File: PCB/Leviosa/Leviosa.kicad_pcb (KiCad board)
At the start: 2 copper layers, 80 x 80 mm, 50 parts, among them J3 Conn_01x03, Q3 TIP122, Q4 TIP122, U1 LM324, U2 ATtiny13A-P, U3 TPS1H200AQDGNRQ1, U5 L7805, U6 SS495A

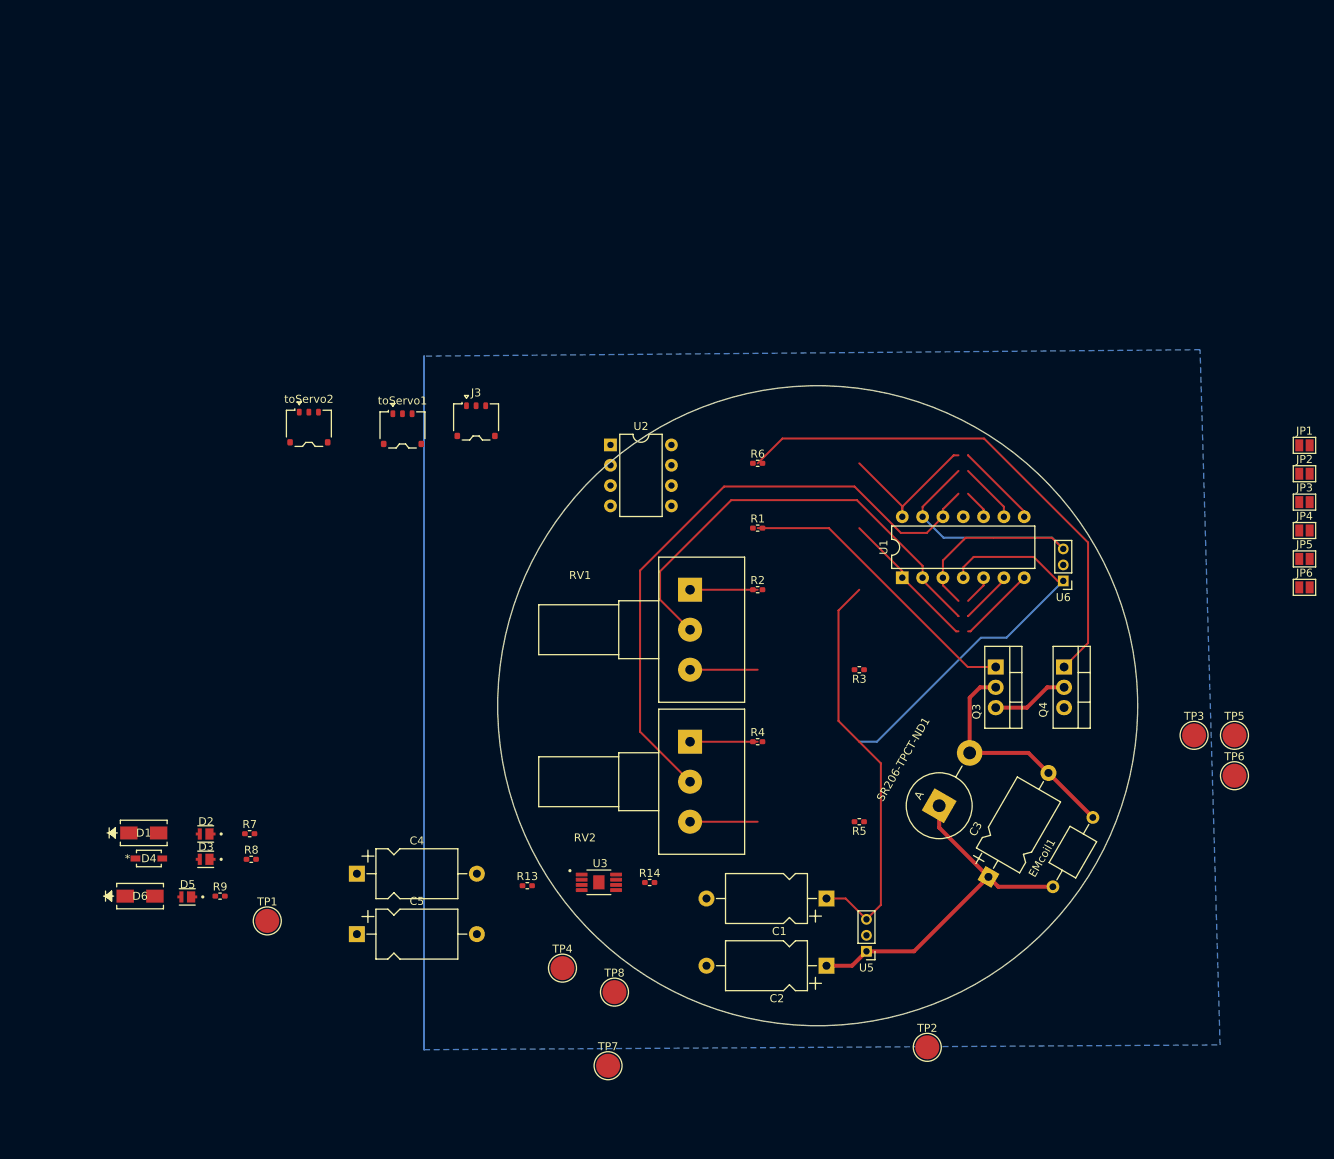
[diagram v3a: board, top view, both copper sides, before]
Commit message: update diode footprint
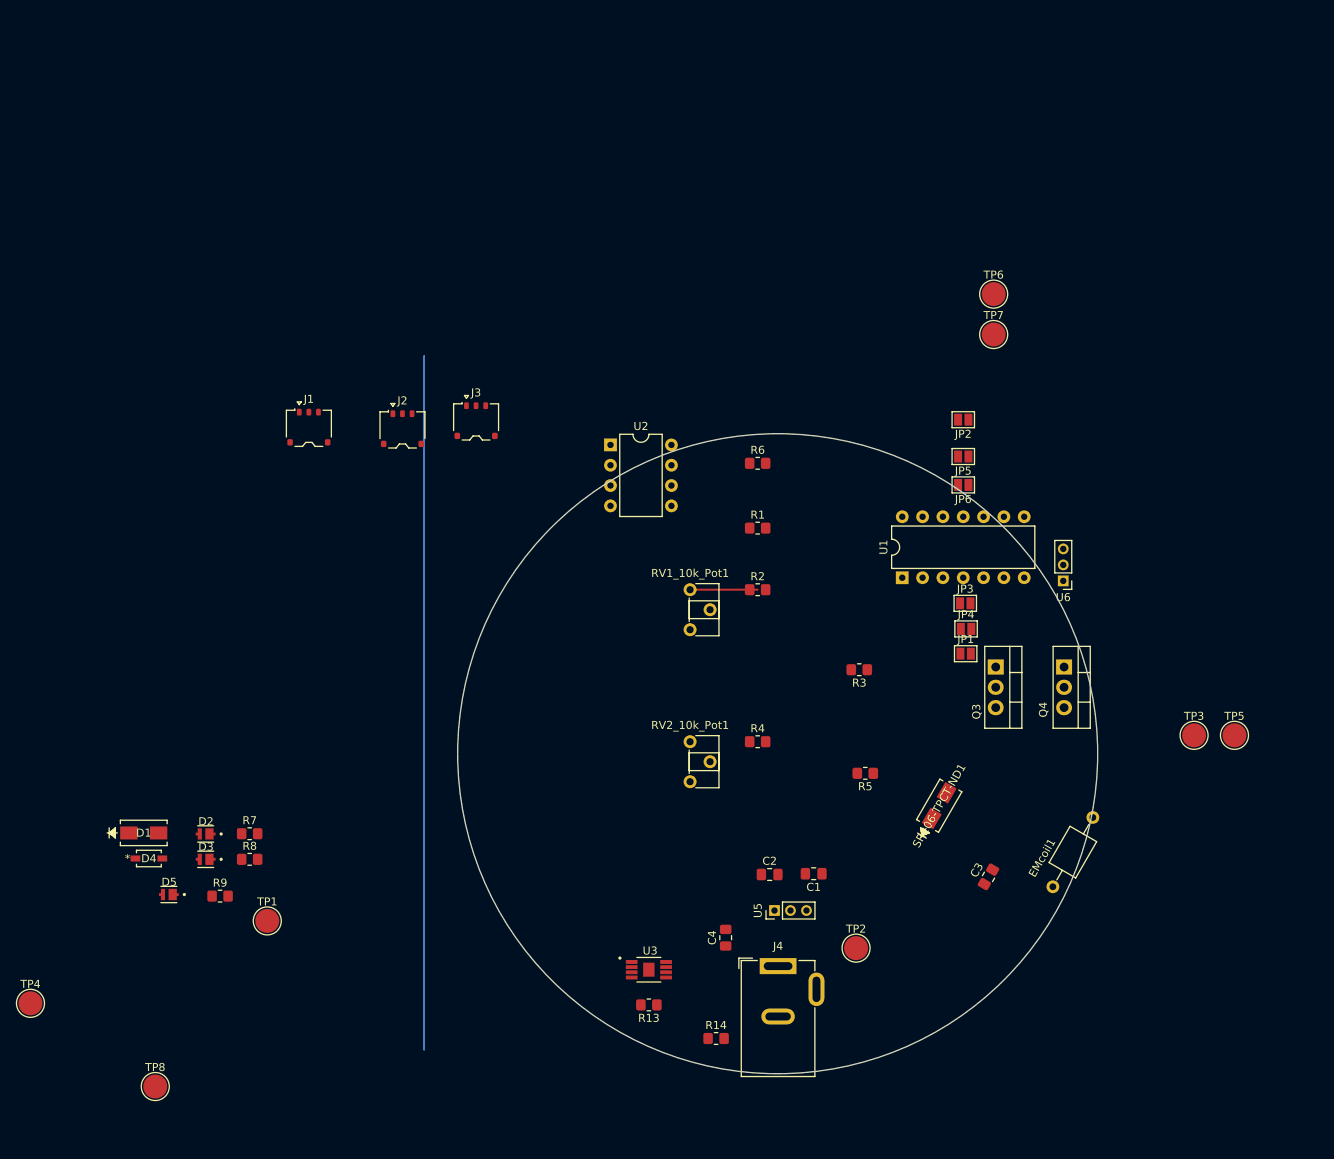
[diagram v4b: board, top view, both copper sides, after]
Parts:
- removed C5: 10µF, Capacitor_THT:CP_Axial_L10.0mm_D6.0mm_P15.00mm_Horizontal
- removed D6: D_Zener, SMAZ9V1-13-F:SMA_DIO
- added J4: Barrel_Jack, Connector_BarrelJack:BarrelJack_GCT_DCJ200-10-A_Horizontal, F.Cu at (160.1, 146.6)
- C1, C2, C3, C4: footprint Capacitor_THT:CP_Axial_L10.0mm_D6.0mm_P15.00mm_Horizontal -> Capacitor_SMD:C_0805_2012Metric_Pad1.18x1.45mm_HandSolder
- J1: renamed from toServo2; value Conn_01x03 -> JST servo 2
- J2: renamed from toServo1; value Conn_01x03 -> JST Servo 1
- J3: value Conn_01x03 -> JST spare
- R1, R13, R14, R2, R3, R4, R6, R7, R8: footprint Resistor_SMD:R_0402_1005Metric_Pad0.72x0.64mm_HandSolder -> Resistor_SMD:R_0805_2012Metric_Pad1.20x1.40mm_HandSolder
- R5: value 54kΩ -> 54.2kΩ; footprint Resistor_SMD:R_0402_1005Metric_Pad0.72x0.64mm_HandSolder -> Resistor_SMD:R_0805_2012Metric_Pad1.20x1.40mm_HandSolder
- R9: value 1kΩ -> 2k4; footprint Resistor_SMD:R_0402_1005Metric_Pad0.72x0.64mm_HandSolder -> Resistor_SMD:R_0805_2012Metric_Pad1.20x1.40mm_HandSolder
- RV1_10k_Pot1: renamed from RV1; value 10k Pot -> 3362S-1-103LF; footprint Potentiometer_THT:Potentiometer_Alps_RK163_Single_Horizontal -> Potentiometer_THT:Potentiometer_ACP_CA6-H2,5_Horizontal
- RV2_10k_Pot1: renamed from RV2; value 10k Pot -> 3362S-1-103LF; footprint Potentiometer_THT:Potentiometer_Alps_RK163_Single_Horizontal -> Potentiometer_THT:Potentiometer_ACP_CA6-H2,5_Horizontal
- SR206-TPCT-ND1: footprint Diode_THT:D_5KPW_P7.62mm_Vertical_AnodeUp -> B230A_13_F:SMA_DIO
- TP1: value TestPoint -> Vout
- TP2: value TestPoint -> 5V
- TP3: value TestPoint -> GND
- TP4: value TestPoint -> Fault
- TP5: value TestPoint -> coil_out
- TP6: value TestPoint -> set_point_trigger
- TP7: value TestPoint -> no_magnet_point_trigger
- TP8: value TestPoint -> 12V
- moved TP7 103.3 mm to (187.0, 67.6)
- moved TP6 67.3 mm to (187.0, 62.5)
- moved TP4 66.6 mm to (66.6, 151.2)
- moved TP8 58.6 mm to (82.2, 161.6)
- moved JP1 49.7 mm to (183.5, 107.5)
- moved C4 46.8 mm to (153.5, 143.0), turned to 90 degrees
- moved JP5 44.5 mm to (183.2, 82.8), turned to 180 degrees
- moved JP6 44.5 mm to (183.2, 86.4), turned to 180 degrees
- moved JP3 44.2 mm to (183.4, 101.2)
- moved JP4 44.1 mm to (183.6, 104.4)
- moved JP2 43.2 mm to (183.2, 78.2), turned to 180 degrees
- moved R13 21.3 mm to (143.9, 151.4), turned to 180 degrees
- moved R14 21.2 mm to (152.3, 155.6)
- moved TP2 15.3 mm to (169.8, 144.3)
- moved C2 13.4 mm to (159.0, 135.1), turned to 0 degrees
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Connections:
- net /hall_output renamed /PB2
- net Net-(J3-Pin_1) renamed /PB3
- net Net-(J3-Pin_2) renamed /PB4
- net Net-(J3-Pin_3) renamed /PB5
- net Net-(U2-PB0) renamed /servo2_control
- net Net-(U2-PB1) renamed /servo1_control
- D5 pad A: Net-(D6-A) -> Net-(D5-PadA)
- D5 pad C: Net-(D5-PadC) -> GND
- R9 pad 1: Net-(D5-PadC) -> /V_out
- R9 pad 2: GND -> Net-(D5-PadA)
- TP6 pad 1: /transistor1_output -> Net-(Q3-B)
- TP7 pad 1: GND -> Net-(Q4-B)
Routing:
- net /5V: track 100.7 -> 0.00 mm
- net /no_magnet_point: track 78.1 -> 0.00 mm
- net Net-(Q4-B): track 64.8 -> 0.00 mm
- net /set_point: track 57.7 -> 0.00 mm
- net /PB2: track 49.4 -> 0.00 mm
- net +12V: track 44.9 -> 0.00 mm
- net Net-(Q3-B): track 36.9 -> 0.00 mm
- net /coil_output: track 29.4 -> 0.00 mm
- net /no_magnet_point_trigger: track 19.9 -> 0.00 mm
- net /set_point_trigger: track 18.2 -> 0.00 mm
- net /spare_no_magnet_point_trigger: track 10.6 -> 0.00 mm
- net /spare_set_point_trigger: track 9.79 -> 0.00 mm
- net /transistor1_output: track 9.60 -> 0.00 mm
- net Net-(R5-Pad2): track 8.45 -> 0.00 mm
- net Net-(R4-Pad1): track 8.45 -> 0.00 mm
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- removed copper zone on B.Cu, net GND

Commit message: update pcb
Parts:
- moved TP8 88.3 mm to (169.8, 150.9)
- moved TP4 86.2 mm to (150.6, 132.0)
- moved R9 85.8 mm to (176.1, 136.8)
- moved D5 85.8 mm to (169.7, 136.6)
- moved TP1 70.5 mm to (166.1, 132.3)
- moved D1 63.1 mm to (140.7, 149.6)
- moved D4 62.6 mm to (144.0, 135.3), turned to 180 degrees
- moved D2 62.0 mm to (147.3, 149.6)
- moved R7 62.0 mm to (152.8, 149.6)
- moved R1 49.9 mm to (207.3, 95.0)
- moved R6 49.9 mm to (207.3, 86.9)
- moved D3 48.4 mm to (136.9, 135.2), turned to 180 degrees
- moved U6 47.2 mm to (148.9, 92.1)
- moved R8 37.5 mm to (131.4, 135.2), turned to 180 degrees
- moved RV1_10k_Pot1 30.4 mm to (120.8, 110.8)
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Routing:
- net Net-(R2-Pad1): track 9.20 -> 0.00 mm

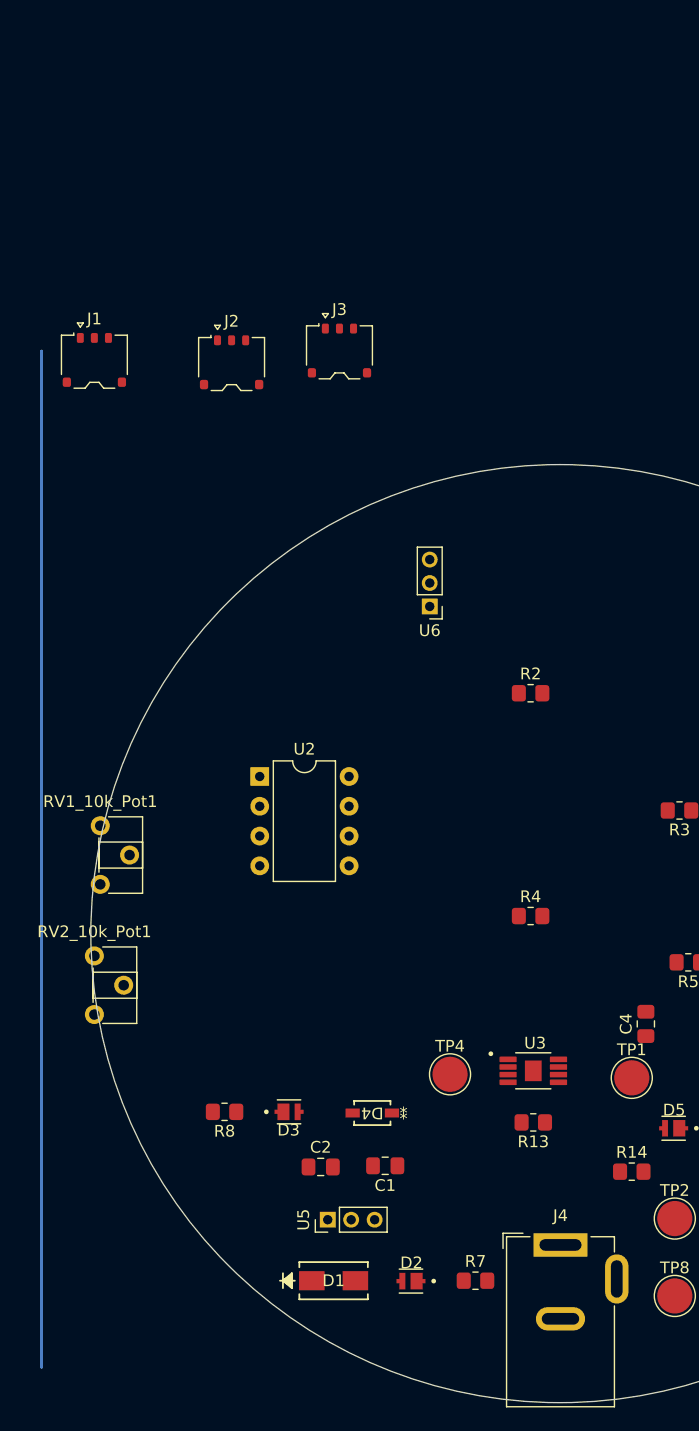
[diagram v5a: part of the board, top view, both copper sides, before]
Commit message: chnagd resistors, didoes and connectors to horizontal common 2.54mm headers
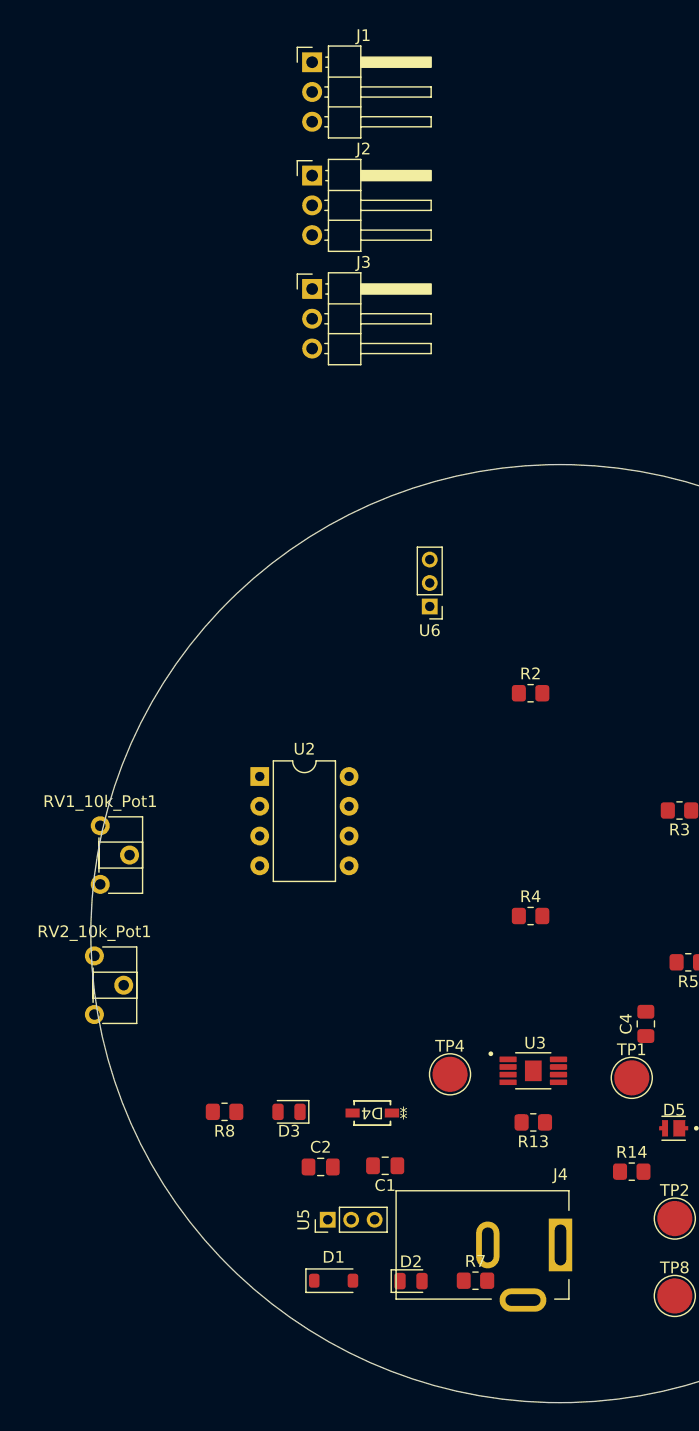
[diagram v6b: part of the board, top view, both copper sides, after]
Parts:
- D1: value D_Zener -> BZT52C8V2 WD; footprint SMAZ9V1-13-F:SMA_DIO -> Diode_SMD:D_SOD-123
- D2, D3: footprint MP-2016-1100-50-70:LED_MP-2016-1100-50-70 -> LED_SMD:LED_0805_2012Metric
- J1: value JST servo 2 -> 2.54mm 1x03 Servo 1; footprint Connector_JST:JST_ACH_BM03B-ACHSS-GAN-ETF_1x03-1MP_P1.20mm_Vertical -> Connector_PinHeader_2.54mm:PinHeader_1x03_P2.54mm_Horizontal
- J2: value JST Servo 1 -> 2.54mm 1x03 Servo 1; footprint Connector_JST:JST_ACH_BM03B-ACHSS-GAN-ETF_1x03-1MP_P1.20mm_Vertical -> Connector_PinHeader_2.54mm:PinHeader_1x03_P2.54mm_Horizontal
- J3: value JST spare -> 2.54mm 1x03 Spare; footprint Connector_JST:JST_ACH_BM03B-ACHSS-GAN-ETF_1x03-1MP_P1.20mm_Vertical -> Connector_PinHeader_2.54mm:PinHeader_1x03_P2.54mm_Horizontal
- J4: footprint Connector_BarrelJack:BarrelJack_GCT_DCJ200-10-A_Horizontal -> Connector_BarrelJack:BarrelJack_Kycon_KLDX-0202-xC_Horizontal
- R8: value 1kΩ -> 400
- moved J1 31.5 mm to (138.9, 45.7)
- moved J2 17.3 mm to (138.9, 55.4)
- moved J3 5.74 mm to (138.9, 65.0)
